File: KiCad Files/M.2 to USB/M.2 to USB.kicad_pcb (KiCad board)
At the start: 4 copper layers, 22 x 26 mm, 33 parts, among them J1 M.2 A+E Key Connector, J2 Conn_2Rows-09Pins_ALT, U1 USB2422T_MJ, U2 AP2152SG-13, U3 MIC2876-5.0, U4 SN74LVC1G14DBVR, Y1 OSC24M-3.3I/S3

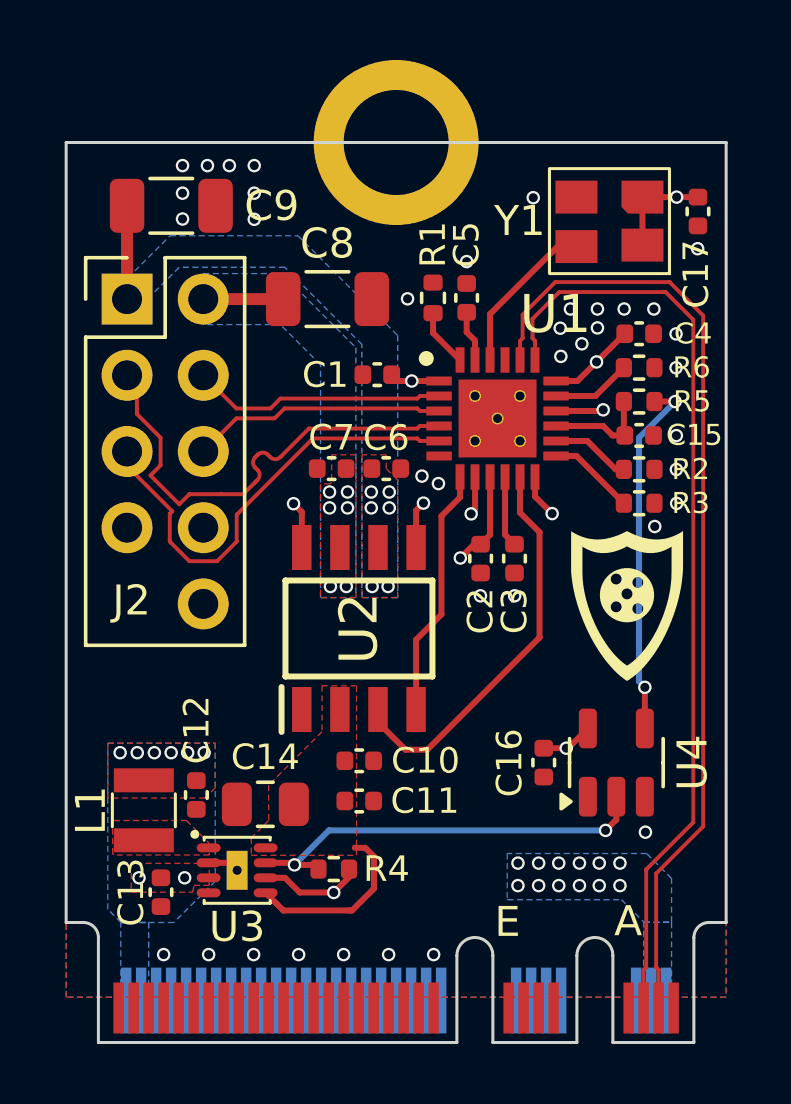
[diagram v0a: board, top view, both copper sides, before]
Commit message: New Renders and updated board
updated the footprints for usb2422, clock chip and m.2 connector.

made new 2D and 3D renders of updated board.
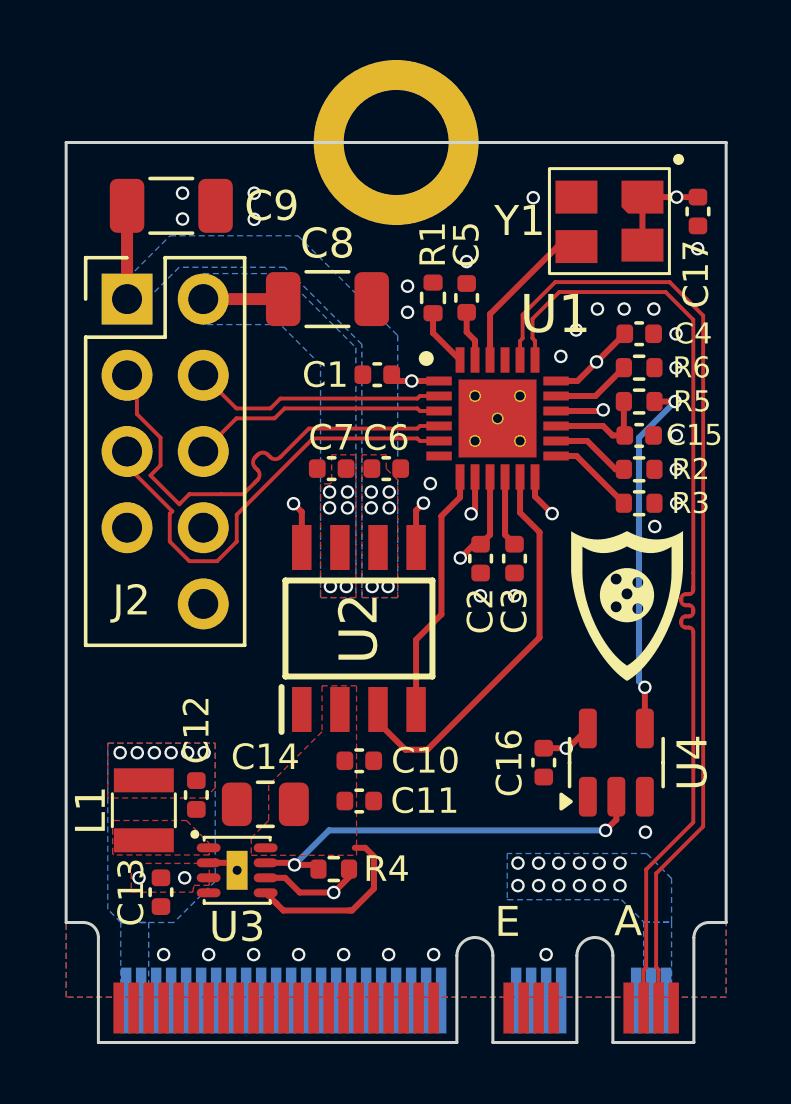
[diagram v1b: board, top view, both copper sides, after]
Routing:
- net USBUP_D-: track 31.1 -> 32.2 mm
- net GND: vias 38 -> 32

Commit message: Updated v1.1 design
-updated v1.1 design
-finished schematic, pcb, render, gerber, and BOM
-removed old v1.0 files
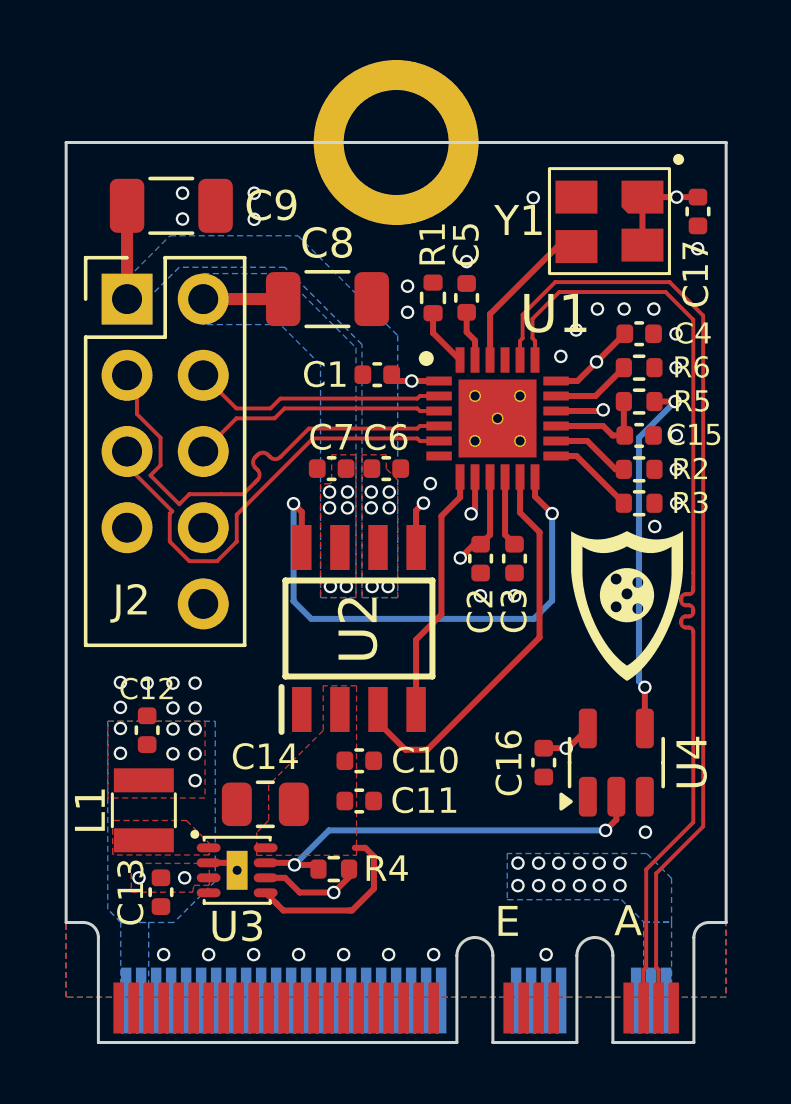
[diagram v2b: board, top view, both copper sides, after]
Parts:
- moved C12 2.71 mm to (125.7, 144.7), turned to 90 degrees
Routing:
- net ~{FLT2}: track 12.3 -> 18.3 mm
- net GND: vias 32 -> 39
- net +3.3V: vias 27 -> 28
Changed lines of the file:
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@@
 	(footprint "Capacitor_SMD:C_0402_1005Metric"
 		(layer "F.Cu")
-		(at 127.34 146.88 -90)
+		(at 125.7 144.72 90)
 		(descr "Capacitor SMD 0402 (1005 Metric), square (rectangular) end terminal, IPC-7351 nominal, (Body size source: IPC-SM-782 page 76, https://www.pcb-3d.com/wordpress/wp-content/uploads/ipc-sm-782a_amendment_1_and_2.pdf), generated with kicad-footprint-generator")
 		(tags "capacitor")
 		(property "Reference" "C12"
-			(at -2.17 -0.01 90)
+			(at 1.36 0 0)
 			(layer "F.SilkS")
 			(effects
 				(font
-					(size 0.85 0.85)
+					(size 0.7 0.7)
 					(thickness 0.15)
 				)
@@
 		(attr smd)
 		(fp_line
-			(start -0.107836 0.36)
-			(end 0.107836 0.36)
+			(start -0.107836 -0.36)
+			(end 0.107836 -0.36)
 			(stroke
 				(width 0.12)
@@
 		)
 		(fp_line
-			(start -0.107836 -0.36)
-			(end 0.107836 -0.36)
+			(start -0.107836 0.36)
+			(end 0.107836 0.36)
 			(stroke
 				(width 0.12)
@@
 		)
 		(fp_line
-			(start -0.91 0.46)
-			(end -0.91 -0.46)
+			(start 0.91 -0.46)
+			(end 0.91 0.46)
 			(stroke
 				(width 0.05)
@@
 		)
 		(fp_line
-			(start 0.91 0.46)
-			(end -0.91 0.46)
+			(start -0.91 -0.46)
+			(end 0.91 -0.46)
 			(stroke
 				(width 0.05)
@@
 		)
 		(fp_line
-			(start -0.91 -0.46)
-			(end 0.91 -0.46)
+			(start 0.91 0.46)
+			(end -0.91 0.46)
 			(stroke
 				(width 0.05)
@@
 		)
 		(fp_line
-			(start 0.91 -0.46)
-			(end 0.91 0.46)
+			(start -0.91 0.46)
+			(end -0.91 -0.46)
 			(stroke
 				(width 0.05)
@@
 		)
 		(fp_line
-			(start -0.5 0.25)
-			(end -0.5 -0.25)
+			(start 0.5 -0.25)
+			(end 0.5 0.25)
 			(stroke
 				(width 0.1)
@@
 		)
 		(fp_line
-			(start 0.5 0.25)
-			(end -0.5 0.25)
+			(start -0.5 -0.25)
+			(end 0.5 -0.25)
 			(stroke
 				(width 0.1)
@@
 		)
 		(fp_line
-			(start -0.5 -0.25)
-			(end 0.5 -0.25)
+			(start 0.5 0.25)
+			(end -0.5 0.25)
 			(stroke
 				(width 0.1)
@@
 		)
 		(fp_line
-			(start 0.5 -0.25)
-			(end 0.5 0.25)
+			(start -0.5 0.25)
+			(end -0.5 -0.25)
 			(stroke
 				(width 0.1)
@@
 		)
 		(pad "1" smd roundrect
-			(at -0.48 0 270)
+			(at -0.48 0 90)
 			(size 0.56 0.62)
 			(layers "F.Cu" "F.Mask" "F.Paste")
@@
 		)
 		(pad "2" smd roundrect
-			(at 0.48 0 270)
+			(at 0.48 0 90)
 			(size 0.56 0.62)
 			(layers "F.Cu" "F.Mask" "F.Paste")
@@
 	)
 	(via
-		(at 141.46 149.9)
+		(at 124.81 145.49)
 		(size 0.45)
 		(drill 0.3)
 		(layers "F.Cu" "B.Cu")
-		(free yes)
 		(net 1)
 	)
 	(via
-		(at 138.06 149.9)
+		(at 126.56 144.68)
+		(size 0.45)
+		(drill 0.3)
+		(layers "F.Cu" "B.Cu")
+		(net 1)
+	)
+	(via
+		(at 127.3 144.68)
+		(size 0.45)
+		(drill 0.3)
+		(layers "F.Cu" "B.Cu")
+		(net 1)
+	)
+	(via
+		(at 141.46 149.9)
 		(size 0.45)
 		(drill 0.3)
@@
 	)
 	(via
-		(at 140.11 149.9)
+		(at 138.06 149.9)
 		(size 0.45)
 		(drill 0.3)
@@
 	)
 	(via
-		(at 141.46 149.15)
+		(at 140.11 149.9)
 		(size 0.45)
 		(drill 0.3)
@@
 	)
 	(via
-		(at 138.75 149.15)
+		(at 141.46 149.15)
 		(size 0.45)
 		(drill 0.3)
@@
 	)
 	(via
-		(at 127.05 145.47)
+		(at 138.75 149.15)
 		(size 0.45)
 		(drill 0.3)
@@
 	)
 	(via
-		(at 124.8 145.47)
+		(at 127.3 145.51)
 		(size 0.45)
 		(drill 0.3)
 		(layers "F.Cu" "B.Cu")
-		(free yes)
 		(net 1)
 	)
 	(via
-		(at 125.37 145.47)
+		(at 124.81 144.66)
 		(size 0.45)
 		(drill 0.3)
 		(layers "F.Cu" "B.Cu")
-		(free yes)
 		(net 1)
 	)
 	(via
-		(at 125.94 145.47)
+		(at 126.56 145.51)
 		(size 0.45)
 		(drill 0.3)
 		(layers "F.Cu" "B.Cu")
-		(free yes)
 		(net 1)
 	)
 	(via
-		(at 140.77 149.9)
+		(at 127.3 146.4)
 		(size 0.45)
 		(drill 0.3)
 		(layers "F.Cu" "B.Cu")
-		(free yes)
 		(net 1)
 	)
 	(via
-		(at 138.06 149.15)
+		(at 140.77 149.9)
 		(size 0.45)
 		(drill 0.3)
@@
 	)
 	(via
-		(at 140.11 149.15)
+		(at 138.06 149.15)
 		(size 0.45)
 		(drill 0.3)
@@
 	)
 	(via
-		(at 126.5 145.47)
+		(at 140.11 149.15)
 		(size 0.45)
 		(drill 0.3)
@@
 		(net 1)
 	)
-	(via
-		(at 127.6 145.47)
-		(size 0.45)
-		(drill 0.3)
-		(layers "F.Cu" "B.Cu")
-		(free yes)
-		(net 1)
-	)
 	(segment
 		(start 128.45 149.14)
@@
 	)
 	(via
+		(at 125.7 143.15)
+		(size 0.45)
+		(drill 0.3)
+		(layers "F.Cu" "B.Cu")
+		(net 2)
+	)
+	(via
 		(at 132.25 152.2)
 		(size 0.45)
@@
 	)
 	(via
+		(at 126.56 143.98)
+		(size 0.45)
+		(drill 0.3)
+		(layers "F.Cu" "B.Cu")
+		(net 2)
+	)
+	(via
 		(at 143.33 132.64)
 		(size 0.45)
@@
 	)
 	(via
+		(at 124.81 143.96)
+		(size 0.45)
+		(drill 0.3)
+		(layers "F.Cu" "B.Cu")
+		(net 2)
+	)
+	(via
 		(at 139 152.2)
 		(size 0.45)
@@
 	)
 	(via
+		(at 124.81 143.13)
+		(size 0.45)
+		(drill 0.3)
+		(layers "F.Cu" "B.Cu")
+		(net 2)
+	)
+	(via
 		(at 126.88 126.82)
 		(size 0.45)
@@
 	)
 	(via
+		(at 127.3 143.98)
+		(size 0.45)
+		(drill 0.3)
+		(layers "F.Cu" "B.Cu")
+		(net 2)
+	)
+	(via
 		(at 129.25 152.2)
 		(size 0.45)
@@
 	)
 	(via
+		(at 127.3 143.15)
+		(size 0.45)
+		(drill 0.3)
+		(layers "F.Cu" "B.Cu")
+		(net 2)
+	)
+	(via
 		(at 135.25 152.2)
 		(size 0.45)
@@
 	)
 	(via
+		(at 126.56 143.15)
+		(size 0.45)
+		(drill 0.3)
+		(layers "F.Cu" "B.Cu")
+		(net 2)
+	)
+	(via
 		(at 141.6 130.68)
 		(size 0.45)
@@
 	)
 	(segment
-		(start 131.56 138.15)
-		(end 138.55 138.15)
+		(start 130.58 137.17)
+		(end 130.58 140.42)
 		(width 0.2)
-		(layer "In2.Cu")
+		(layer "B.Cu")
 		(net 65)
 	)
 	(segment
-		(start 138.55 138.15)
+		(start 139.2 140.4)
 		(end 139.2 137.5)
 		(width 0.2)
-		(layer "In2.Cu")
+		(layer "B.Cu")
 		(net 65)
 	)
 	(segment
-		(start 130.58 137.17)
-		(end 131.56 138.15)
+		(start 131.17 141.01)
+		(end 138.59 141.01)
 		(width 0.2)
-		(layer "In2.Cu")
+		(layer "B.Cu")
+		(net 65)
+	)
+	(segment
+		(start 130.58 140.42)
+		(end 131.17 141.01)
+		(width 0.2)
+		(layer "B.Cu")
+		(net 65)
+	)
+	(segment
+		(start 138.59 141.01)
+		(end 139.2 140.4)
+		(width 0.2)
+		(layer "B.Cu")
 		(net 65)
 	)
@@
 		(polygon
 			(pts
-				(xy 129.17 148.89) (xy 132.68 148.89) (xy 132.68 143.24) (xy 131.53 143.24) (xy 131.53 144.77) (xy 129.75 146.55)
-				(xy 129.75 147.73) (xy 129.17 148.31)
+				(xy 129.35 148.89) (xy 132.68 148.89) (xy 132.68 143.24) (xy 131.57 143.24) (xy 131.57 144.73) (xy 129.75 146.55)
+				(xy 129.75 147.73) (xy 129.35 148.13)
 			)
 		)
@@
 		(polygon
 			(pts
-				(xy 124.39 145.15) (xy 127.97 145.15) (xy 127.97 146.64) (xy 127.63 146.98) (xy 124.39 146.98)
+				(xy 124.39 144.42) (xy 127.63 144.42) (xy 127.63 146.98) (xy 124.39 146.98)
 			)
 		)
@@
 		(polygon
 			(pts
-				(xy 124.83 151.13) (xy 124.39 150.69) (xy 124.39 145.15) (xy 127.97 145.15) (xy 127.97 149.75) (xy 126.59 151.13)
+				(xy 124.83 151.13) (xy 124.39 150.69) (xy 124.39 144.42) (xy 127.97 144.42) (xy 127.97 149.75) (xy 126.59 151.13)
 			)
 		)
@@
 			(pts
 				(xy 131.62 150.47) (xy 131.15 150) (xy 131.15 148.04) (xy 129.23 146.12) (xy 124.59 146.12) (xy 124.25 145.78)
-				(xy 124.25 144.54) (xy 125.27 143.52) (xy 130.72 143.52) (xy 131.11 143.13) (xy 131.11 134.17) (xy 133.68 131.6)
-				(xy 134.19 131.6) (xy 137 128.79) (xy 137 126.53) (xy 137.55 125.98) (xy 144.01 125.98) (xy 144.51 126.48)
-				(xy 144.51 147.73) (xy 141.77 150.47)
+				(xy 124.25 144.43) (xy 129.81 144.43) (xy 131.11 143.13) (xy 131.11 134.17) (xy 133.68 131.6) (xy 134.19 131.6)
+				(xy 137 128.79) (xy 137 126.53) (xy 137.55 125.98) (xy 144.01 125.98) (xy 144.51 126.48) (xy 144.51 147.73)
+				(xy 141.77 150.47)
 			)
 		)

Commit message: fixed vbus nets
vbus nets were corrected so flt/en port from the hub lined up with the usb port on the header
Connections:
- C6 pad 1: VBUS1 -> VBUS2
- C7 pad 2: VBUS2 -> VBUS1
- C8 pad 1: VBUS2 -> VBUS1
- C9 pad 2: VBUS1 -> VBUS2
- J2 pad 1: VBUS1 -> VBUS2
- J2 pad 2: VBUS2 -> VBUS1
- U2 pad 3: PRTEN2 -> PRTEN1
- U2 pad 4: PRTEN1 -> PRTEN2
- U2 pad 5: ~{FLT1} -> ~{FLT2}
- U2 pad 6: VBUS1 -> VBUS2
- U2 pad 7: VBUS2 -> VBUS1
- U2 pad 8: ~{FLT2} -> ~{FLT1}
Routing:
- net ~{FLT2}: track 18.3 -> 7.61 mm
- net ~{FLT1}: track 4.60 -> 9.19 mm
- net PRTEN2: track 13.4 -> 10.0 mm
- net PRTEN1: track 8.36 -> 9.31 mm
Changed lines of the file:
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@@
 			(layers "*.Cu" "*.Mask")
 			(remove_unused_layers no)
-			(net 6 "VBUS1")
+			(net 5 "VBUS2")
 			(pinfunction "Pin_1")
 			(pintype "passive")
@@
 			(layers "*.Cu" "*.Mask")
 			(remove_unused_layers no)
-			(net 5 "VBUS2")
+			(net 6 "VBUS1")
 			(pinfunction "Pin_2")
 			(pintype "passive")
@@
 			(layers "F.Cu" "F.Mask" "F.Paste")
 			(roundrect_rratio 0.25)
-			(net 5 "VBUS2")
+			(net 6 "VBUS1")
 			(pintype "passive")
 		)
@@
 			(size 0.65 1.5)
 			(layers "F.Cu" "F.Mask" "F.Paste")
-			(net 66 "PRTEN2")
+			(net 69 "PRTEN1")
 			(pinfunction "EN1")
 			(pintype "input")
@@
 			(size 0.65 1.5)
 			(layers "F.Cu" "F.Mask" "F.Paste")
-			(net 69 "PRTEN1")
+			(net 66 "PRTEN2")
 			(pinfunction "EN2")
 			(pintype "input")
@@
 			(size 0.65 1.5)
 			(layers "F.Cu" "F.Mask" "F.Paste")
-			(net 64 "~{FLT1}")
+			(net 65 "~{FLT2}")
 			(pinfunction "FLG2")
 			(pintype "output")
@@
 			(size 0.65 1.5)
 			(layers "F.Cu" "F.Mask" "F.Paste")
-			(net 6 "VBUS1")
+			(net 5 "VBUS2")
 			(pinfunction "OUT2")
 			(pintype "output")
@@
 			(size 0.65 1.5)
 			(layers "F.Cu" "F.Mask" "F.Paste")
-			(net 5 "VBUS2")
+			(net 6 "VBUS1")
 			(pinfunction "OUT1")
 			(pintype "output")
@@
 			(size 0.65 1.5)
 			(layers "F.Cu" "F.Mask" "F.Paste")
-			(net 65 "~{FLT2}")
+			(net 64 "~{FLT1}")
 			(pinfunction "FLG1")
 			(pintype "output")
@@
 			(layers "F.Cu" "F.Mask" "F.Paste")
 			(roundrect_rratio 0.217391)
-			(net 5 "VBUS2")
+			(net 6 "VBUS1")
 			(pintype "passive")
 		)
@@
 			(layers "F.Cu" "F.Mask" "F.Paste")
 			(roundrect_rratio 0.217391)
-			(net 6 "VBUS1")
+			(net 5 "VBUS2")
 			(pintype "passive")
 		)
@@
 			(layers "F.Cu" "F.Mask" "F.Paste")
 			(roundrect_rratio 0.25)
-			(net 6 "VBUS1")
+			(net 5 "VBUS2")
 			(pintype "passive")
 		)
@@
 	)
 	(segment
-		(start 127.57 130.35)
-		(end 130.235 130.35)
+		(start 125.03 127.24)
+		(end 125.03 130.35)
 		(width 0.4)
 		(layer "F.Cu")
@@
 	)
 	(via
-		(at 131.78 137.31)
+		(at 133.77 136.78)
 		(size 0.45)
 		(drill 0.3)
@@
 	)
 	(via
-		(at 132.38 137.31)
+		(at 133.17 136.78)
 		(size 0.45)
 		(drill 0.3)
@@
 	)
 	(via
-		(at 132.34 139.93)
+		(at 133.73 139.93)
 		(size 0.45)
 		(drill 0.3)
@@
 	)
 	(via
-		(at 131.81 139.93)
+		(at 133.17 137.31)
 		(size 0.45)
 		(drill 0.3)
@@
 	)
 	(via
-		(at 131.78 136.78)
+		(at 133.77 137.31)
 		(size 0.45)
 		(drill 0.3)
@@
 	)
 	(via
-		(at 132.38 136.78)
+		(at 133.2 139.93)
 		(size 0.45)
 		(drill 0.3)
@@
 	)
 	(segment
-		(start 125.03 127.24)
-		(end 125.03 130.35)
+		(start 127.57 130.35)
+		(end 130.235 130.35)
 		(width 0.4)
 		(layer "F.Cu")
@@
 	)
 	(via
-		(at 133.77 136.78)
+		(at 131.78 137.31)
 		(size 0.45)
 		(drill 0.3)
@@
 	)
 	(via
-		(at 133.17 136.78)
+		(at 132.38 137.31)
 		(size 0.45)
 		(drill 0.3)
@@
 	)
 	(via
-		(at 133.73 139.93)
+		(at 132.34 139.93)
 		(size 0.45)
 		(drill 0.3)
@@
 	)
 	(via
-		(at 133.17 137.31)
+		(at 131.81 139.93)
 		(size 0.45)
 		(drill 0.3)
@@
 	)
 	(via
-		(at 133.77 137.31)
+		(at 131.78 136.78)
 		(size 0.45)
 		(drill 0.3)
@@
 	)
 	(via
-		(at 133.2 139.93)
+		(at 132.38 136.78)
 		(size 0.45)
 		(drill 0.3)
@@
 	)
 	(segment
-		(start 134.665 137.395)
-		(end 134.91 137.15)
+		(start 130.855 137.445)
+		(end 130.58 137.17)
 		(width 0.2)
 		(layer "F.Cu")
@@
 	)
 	(segment
-		(start 136.63 137.38)
-		(end 136.5 137.51)
+		(start 130.855 138.63)
+		(end 130.855 137.445)
 		(width 0.2)
 		(layer "F.Cu")
@@
 	)
 	(segment
-		(start 134.665 138.63)
-		(end 134.665 137.395)
+		(start 136.63 137.38)
+		(end 136.5 137.51)
 		(width 0.2)
 		(layer "F.Cu")
@@
 	)
 	(via
-		(at 136.5 137.51)
+		(at 130.58 137.17)
 		(size 0.45)
 		(drill 0.3)
@@
 	)
 	(via
-		(at 134.91 137.15)
+		(at 136.5 137.51)
 		(size 0.45)
 		(drill 0.3)
@@
 	)
 	(segment
-		(start 134.91 137.15)
-		(end 136.14 137.15)
+		(start 136.174 137.836)
+		(end 131.246 137.836)
 		(width 0.2)
 		(layer "In2.Cu")
@@
 	)
 	(segment
-		(start 136.14 137.15)
-		(end 136.5 137.51)
+		(start 131.246 137.836)
+		(end 130.58 137.17)
 		(width 0.2)
 		(layer "In2.Cu")
@@
 	)
 	(segment
-		(start 138.63 136.28)
-		(end 138.63 136.93)
+		(start 136.5 137.51)
+		(end 136.174 137.836)
+		(width 0.2)
+		(layer "In2.Cu")
+		(net 64)
+	)
+	(segment
+		(start 134.665 137.395)
+		(end 134.91 137.15)
 		(width 0.2)
 		(layer "F.Cu")
@@
 	)
 	(segment
-		(start 130.855 137.445)
-		(end 130.58 137.17)
+		(start 138.63 136.28)
+		(end 138.63 136.93)
 		(width 0.2)
 		(layer "F.Cu")
@@
 	)
 	(segment
-		(start 130.855 138.63)
-		(end 130.855 137.445)
+		(start 134.665 138.63)
+		(end 134.665 137.395)
 		(width 0.2)
 		(layer "F.Cu")
@@
 	)
 	(via
-		(at 130.58 137.17)
+		(at 134.91 137.15)
 		(size 0.45)
 		(drill 0.3)
@@
 	)
 	(segment
-		(start 130.58 137.17)
-		(end 130.58 140.42)
-		(width 0.2)
-		(layer "B.Cu")
-		(net 65)
-	)
-	(segment
-		(start 139.2 140.4)
-		(end 139.2 137.5)
+		(start 134.91 137.15)
+		(end 136.116123 137.15)
 		(width 0.2)
 		(layer "B.Cu")
@@
 	)
 	(segment
-		(start 131.17 141.01)
-		(end 138.59 141.01)
+		(start 136.116123 137.15)
+		(end 136.282123 136.984)
 		(width 0.2)
 		(layer "B.Cu")
@@
 	)
 	(segment
-		(start 130.58 140.42)
-		(end 131.17 141.01)
+		(start 136.282123 136.984)
+		(end 138.684 136.984)
 		(width 0.2)
 		(layer "B.Cu")
@@
 	)
 	(segment
-		(start 138.59 141.01)
-		(end 139.2 140.4)
+		(start 138.684 136.984)
+		(end 139.2 137.5)
 		(width 0.2)
 		(layer "B.Cu")
@@
 	)
 	(segment
-		(start 133.395 144.03)
-		(end 133.395 144.455)
+		(start 138.78 140.44)
+		(end 138.78 138.12)
 		(width 0.2)
 		(layer "F.Cu")
@@
 	)
 	(segment
-		(start 135.04 145.37)
-		(end 138.78 141.63)
-		(width 0.2)
-		(layer "F.Cu")
-		(net 66)
-	)
-	(segment
-		(start 134.31 145.37)
-		(end 135.04 145.37)
+		(start 134.665 144.03)
+		(end 135.19 144.03)
 		(width 0.2)
 		(layer "F.Cu")
@@
 	)
 	(segment
-		(start 133.395 144.455)
-		(end 134.31 145.37)
-		(width 0.2)
-		(layer "F.Cu")
-		(net 66)
-	)
-	(segment
-		(start 138.78 141.63)
-		(end 138.78 138.12)
+		(start 135.19 144.03)
+		(end 138.78 140.44)
 		(width 0.2)
 		(layer "F.Cu")
@@
 	)
 	(segment
-		(start 136.13 136.28)
-		(end 136.13 136.96)
+		(start 133.395 144.03)
+		(end 133.395 144.455)
 		(width 0.2)
 		(layer "F.Cu")
@@
 	)
 	(segment
-		(start 135.51 140.86)
-		(end 134.665 141.705)
+		(start 135.51 137.58)
+		(end 135.51 140.305)
 		(width 0.2)
 		(layer "F.Cu")
@@
 	)
 	(segment
-		(start 134.665 141.705)
-		(end 134.665 144.03)
+		(start 133.395 142.42)
+		(end 133.395 144.03)
 		(width 0.2)
 		(layer "F.Cu")
@@
 	)
 	(segment
-		(start 135.51 137.58)
-		(end 135.51 140.86)
+		(start 136.13 136.28)
+		(end 136.13 136.96)
+		(width 0.2)
+		(layer "F.Cu")
+		(net 69)
+	)
+	(segment
+		(start 135.51 140.305)
+		(end 133.395 142.42)
 		(width 0.2)
 		(layer "F.Cu")
@@
 	)
 	(zone
-		(net 5)
-		(net_name "VBUS2")
+		(net 6)
+		(net_name "VBUS1")
 		(layer "F.Cu")
 		(hatch edge 0.5)
@@
 	)
 	(zone
-		(net 6)
-		(net_name "VBUS1")
+		(net 5)
+		(net_name "VBUS2")
 		(layer "F.Cu")
 		(hatch edge 0.5)
@@
 	)
 	(zone
-		(net 6)
-		(net_name "VBUS1")
+		(net 5)
+		(net_name "VBUS2")
 		(layer "B.Cu")
 		(hatch edge 0.5)
@@
 	)
 	(zone
-		(net 5)
-		(net_name "VBUS2")
+		(net 6)
+		(net_name "VBUS1")
 		(layer "B.Cu")
 		(hatch edge 0.5)
